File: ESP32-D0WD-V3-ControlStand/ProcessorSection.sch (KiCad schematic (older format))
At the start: 50 parts, among them J13 USB_OTG, Q1 UMH3N, SW24 RESET, U10 ESP32-D0WD-V3, U11 W25Q32JVSSIQ, U9 FT231XS-R, Y1 40 Mhz +/- 10 ppm

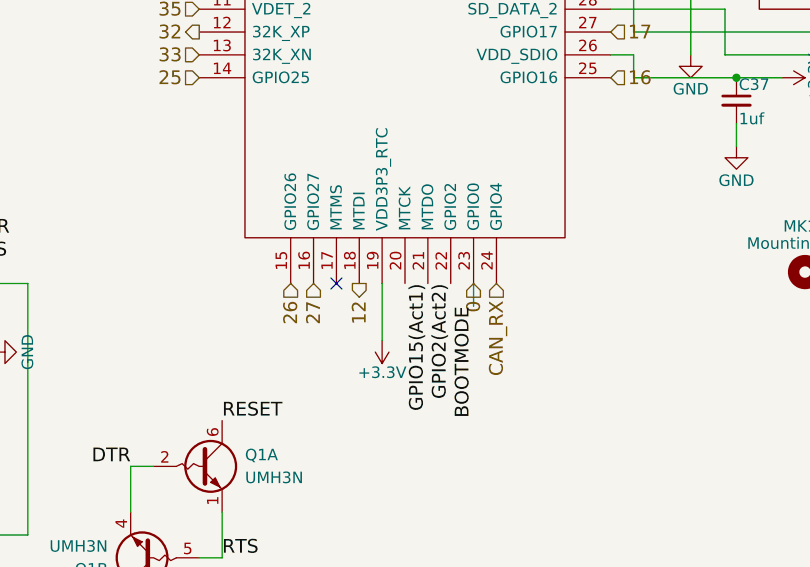
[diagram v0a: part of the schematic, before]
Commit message: Completed V0-1 board (still need to add a few things -- logos and such and adjust silk).
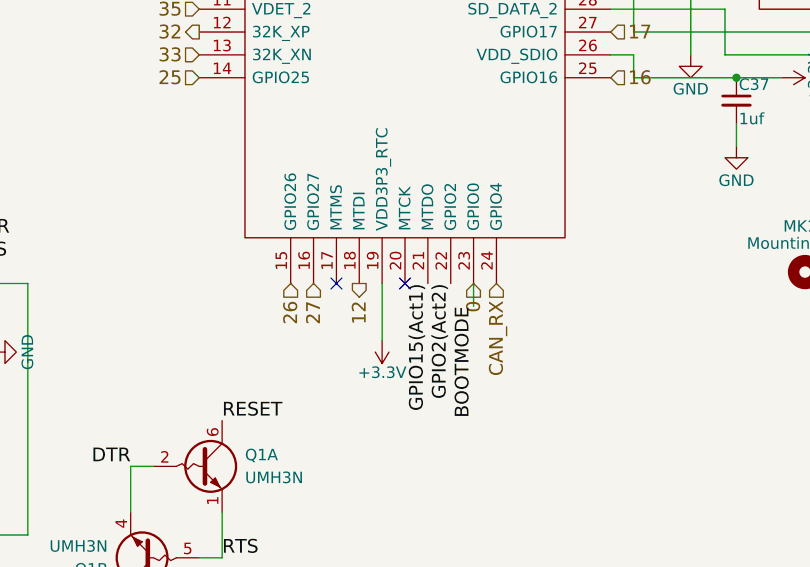
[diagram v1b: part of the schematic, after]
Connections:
- no-connect marks 9 -> 10
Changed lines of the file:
@@
 $EndComp
 NoConn ~ 5450 5400
+NoConn ~ 5750 5400
 $EndSCHEMATC
